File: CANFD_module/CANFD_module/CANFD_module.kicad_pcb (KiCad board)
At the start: 2 copper layers, 26.1 x 37.6 mm, 29 parts, among them SW1 SS-12SDP2, U2 MCP2517FD, U3 AZ1117CH-3.3TRG1, X1 XRCGB40M000F4M01R0

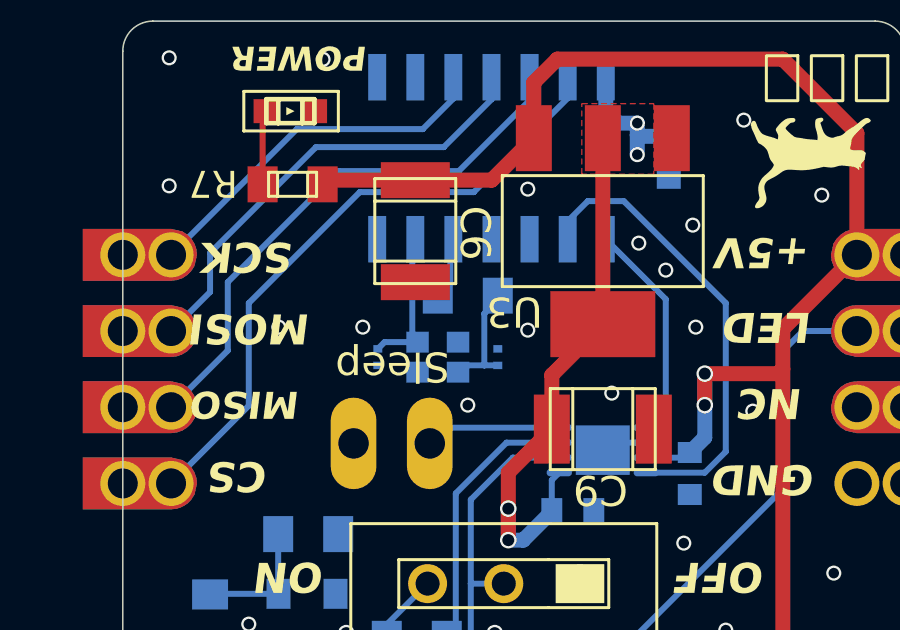
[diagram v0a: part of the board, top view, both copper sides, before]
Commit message: [fix]0603->1608 package
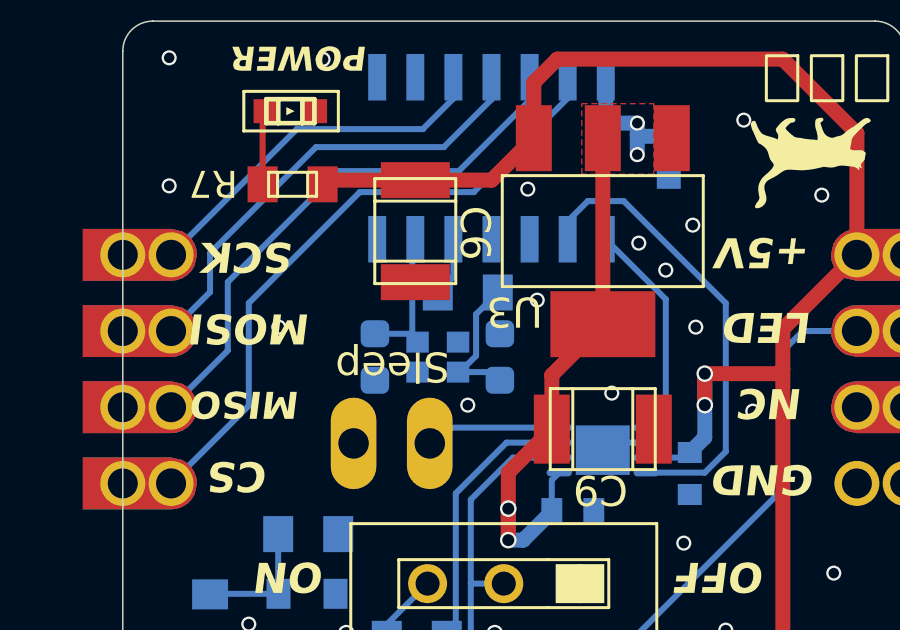
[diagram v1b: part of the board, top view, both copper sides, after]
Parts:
- C4, C5: value GRM0335C1H6R0BA01D -> 1608_SMD; footprint CANFD_module:GRM0335C1H120GA01 -> Capacitor_SMD:C_0603_1608Metric
- moved R1 0.10 mm to (147.0, 95.2)
- moved C5 0.10 mm to (143.9, 97.4)
- moved C4 0.07 mm to (148.0, 97.4)
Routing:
- net N$42: track 3.93 -> 5.31 mm
- net SGND: vias 30 -> 29
